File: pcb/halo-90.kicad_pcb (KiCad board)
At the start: 4 copper layers, 24 x 28.2 mm, 102 parts, among them J1 TC2030-SWIM-NL, U1 UFQFPN28, U3 DRV5032

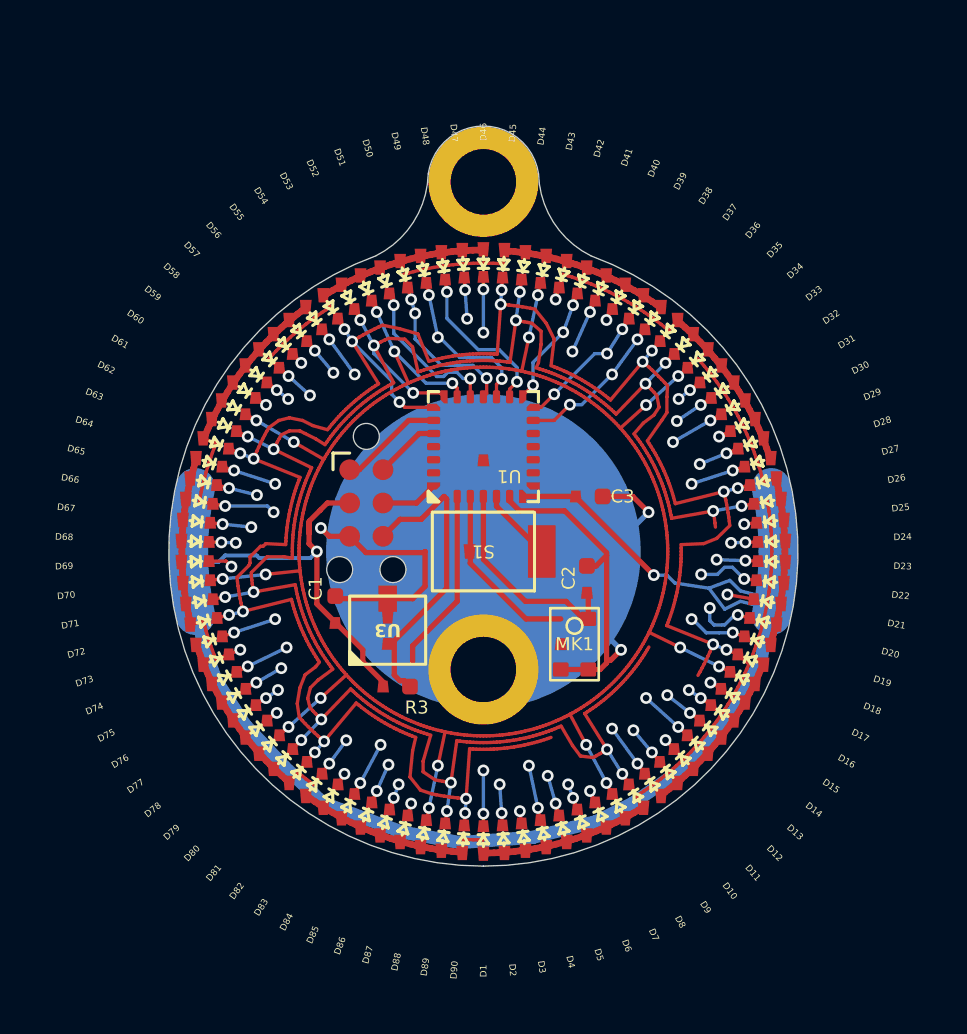
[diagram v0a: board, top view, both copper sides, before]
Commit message: feat(pcb): upgrade to KiCad 9, fix arc syntax, and standardize symbol libraries
- Updated halo.js gr_arc syntax to KiCad 9 (start/mid/end) point-based format.
- Standardized all 13 symbol libraries to KiCad 9 (version 20241209).
- Regenerated halo-90.kicad_pcb with correct formatting and net names.
- Verified file load compatibility.
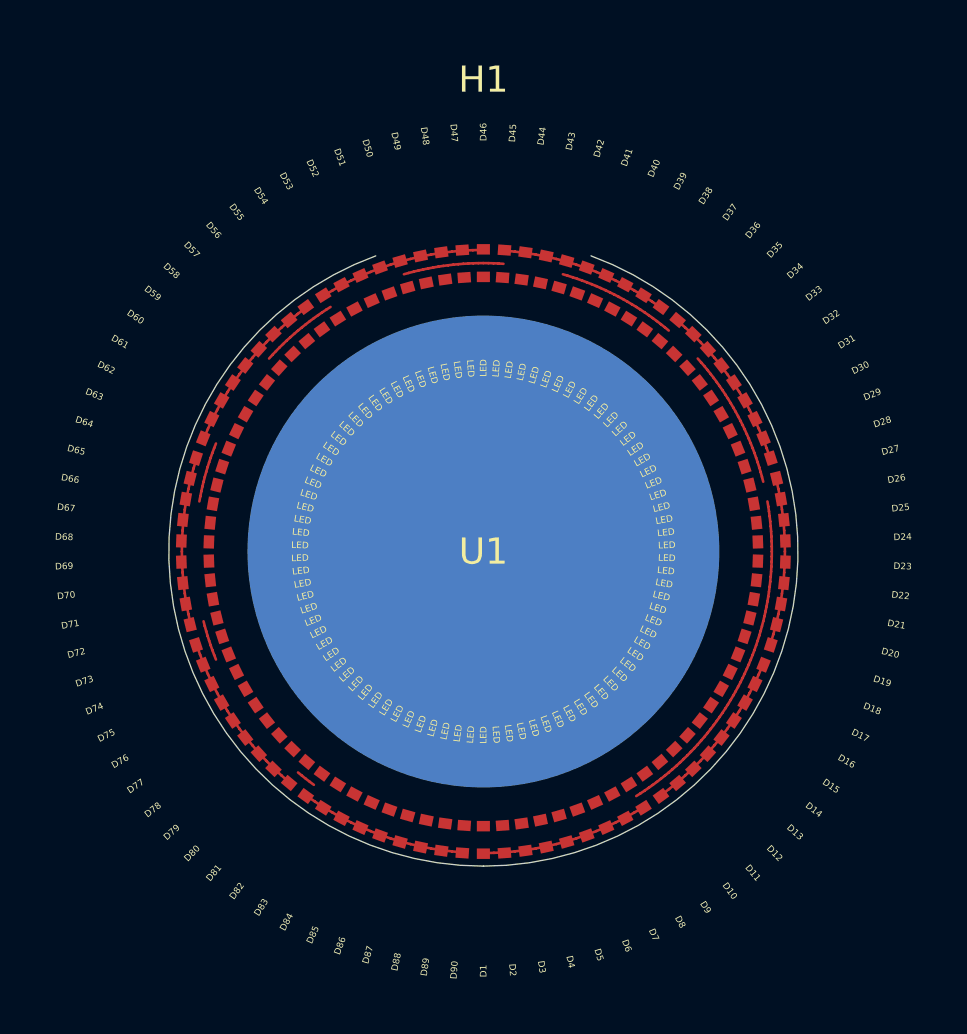
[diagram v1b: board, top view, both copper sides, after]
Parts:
- removed C1: 1u, passives:C-0402
- removed C2, C3: 100n, passives:C-0402
- removed H2: SMTSO1610MTJ, SMTSO1610MTJ:SMTSO1610MTJ
- removed J1: TC2030-SWIM-NL, TC2030-IDC-NL:Tag-Connect_TC2030-IDC-NL_2x03_P1.27mm_Vertical
- removed MK1: ZTS6216, ZTS6216:ZTS6216
- removed R3: 10k, passives:R-0402
- removed S1: TS-1088-AR02016, TS-1088-AR02016L:TS-1088-AR02016
- removed U3: DRV5032, DRV5032:DRV5032
- BT1: value CR-2032 -> CR2032
- H1: value SMTSO1610MTJ -> (none); footprint SMTSO1610MTJ:SMTSO1610MTJ -> earringHookWire:earringHookWire
- U1: value UFQFPN28 -> STM8L15xxx
- moved U1 4.00 mm to (0.00, 0.00), turned to 0 degrees
- moved H1 1.10 mm to (0.00, -13.0)
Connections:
- D1 pad 1: CPX-9 -> CPX-0
- D1 pad 2: CPX-0 -> CPX-9
- D10 pad 1: CPX-9 -> CPX-1
- D10 pad 2: CPX-1 -> CPX-9
- D11 pad 1: CPX-8 -> CPX-1
- D11 pad 2: CPX-1 -> CPX-8
- D12 pad 1: CPX-7 -> CPX-1
- D12 pad 2: CPX-1 -> CPX-7
- D13 pad 1: CPX-6 -> CPX-1
- D13 pad 2: CPX-1 -> CPX-6
- D14 pad 1: CPX-5 -> CPX-1
- D14 pad 2: CPX-1 -> CPX-5
- D15 pad 1: CPX-4 -> CPX-1
- D15 pad 2: CPX-1 -> CPX-4
- D16 pad 1: CPX-3 -> CPX-1
- D16 pad 2: CPX-1 -> CPX-3
- D17 pad 1: CPX-2 -> CPX-1
- D17 pad 2: CPX-1 -> CPX-2
- D18 pad 1: CPX-0 -> CPX-1
- D18 pad 2: CPX-1 -> CPX-0
- D19 pad 1: CPX-9 -> CPX-2
- D19 pad 2: CPX-2 -> CPX-9
- D2 pad 1: CPX-8 -> CPX-0
- D2 pad 2: CPX-0 -> CPX-8
- D20 pad 1: CPX-8 -> CPX-2
- D20 pad 2: CPX-2 -> CPX-8
- D21 pad 1: CPX-7 -> CPX-2
- D21 pad 2: CPX-2 -> CPX-7
- D22 pad 1: CPX-6 -> CPX-2
- D22 pad 2: CPX-2 -> CPX-6
- D23 pad 1: CPX-5 -> CPX-2
- D23 pad 2: CPX-2 -> CPX-5
- D24 pad 1: CPX-4 -> CPX-2
- D24 pad 2: CPX-2 -> CPX-4
- D25 pad 1: CPX-3 -> CPX-2
- D25 pad 2: CPX-2 -> CPX-3
- D26 pad 1: CPX-1 -> CPX-2
- D26 pad 2: CPX-2 -> CPX-1
- D27 pad 1: CPX-0 -> CPX-2
- D27 pad 2: CPX-2 -> CPX-0
- D28 pad 1: CPX-9 -> CPX-3
- D28 pad 2: CPX-3 -> CPX-9
- D29 pad 1: CPX-8 -> CPX-3
- D29 pad 2: CPX-3 -> CPX-8
- D3 pad 1: CPX-7 -> CPX-0
- D3 pad 2: CPX-0 -> CPX-7
- D30 pad 1: CPX-7 -> CPX-3
- D30 pad 2: CPX-3 -> CPX-7
- D31 pad 1: CPX-6 -> CPX-3
- D31 pad 2: CPX-3 -> CPX-6
- D32 pad 1: CPX-5 -> CPX-3
- D32 pad 2: CPX-3 -> CPX-5
- D33 pad 1: CPX-4 -> CPX-3
- D33 pad 2: CPX-3 -> CPX-4
- D34 pad 1: CPX-2 -> CPX-3
- D34 pad 2: CPX-3 -> CPX-2
- D35 pad 1: CPX-1 -> CPX-3
- D35 pad 2: CPX-3 -> CPX-1
- D36 pad 1: CPX-0 -> CPX-3
- D36 pad 2: CPX-3 -> CPX-0
- D37 pad 1: CPX-9 -> CPX-4
- D37 pad 2: CPX-4 -> CPX-9
- D38 pad 1: CPX-8 -> CPX-4
- D38 pad 2: CPX-4 -> CPX-8
- D39 pad 1: CPX-7 -> CPX-4
- D39 pad 2: CPX-4 -> CPX-7
- D4 pad 1: CPX-6 -> CPX-0
- D4 pad 2: CPX-0 -> CPX-6
- D40 pad 1: CPX-6 -> CPX-4
- D40 pad 2: CPX-4 -> CPX-6
- D41 pad 1: CPX-5 -> CPX-4
- D41 pad 2: CPX-4 -> CPX-5
- D42 pad 1: CPX-3 -> CPX-4
- D42 pad 2: CPX-4 -> CPX-3
- D43 pad 1: CPX-2 -> CPX-4
- D43 pad 2: CPX-4 -> CPX-2
- D44 pad 1: CPX-1 -> CPX-4
- D44 pad 2: CPX-4 -> CPX-1
- D45 pad 1: CPX-0 -> CPX-4
- D45 pad 2: CPX-4 -> CPX-0
- D46 pad 1: CPX-9 -> CPX-5
- D46 pad 2: CPX-5 -> CPX-9
- D47 pad 1: CPX-8 -> CPX-5
- D47 pad 2: CPX-5 -> CPX-8
- D48 pad 1: CPX-7 -> CPX-5
- D48 pad 2: CPX-5 -> CPX-7
- D49 pad 1: CPX-6 -> CPX-5
- D49 pad 2: CPX-5 -> CPX-6
- D5 pad 1: CPX-5 -> CPX-0
- D5 pad 2: CPX-0 -> CPX-5
- D50 pad 1: CPX-4 -> CPX-5
- D50 pad 2: CPX-5 -> CPX-4
- D51 pad 1: CPX-3 -> CPX-5
- D51 pad 2: CPX-5 -> CPX-3
- D52 pad 1: CPX-2 -> CPX-5
- D52 pad 2: CPX-5 -> CPX-2
- D53 pad 1: CPX-1 -> CPX-5
- D53 pad 2: CPX-5 -> CPX-1
- D54 pad 1: CPX-0 -> CPX-5
- D54 pad 2: CPX-5 -> CPX-0
- D55 pad 1: CPX-9 -> CPX-6
- D55 pad 2: CPX-6 -> CPX-9
- D56 pad 1: CPX-8 -> CPX-6
- D56 pad 2: CPX-6 -> CPX-8
- D57 pad 1: CPX-7 -> CPX-6
- D57 pad 2: CPX-6 -> CPX-7
- D58 pad 1: CPX-5 -> CPX-6
- D58 pad 2: CPX-6 -> CPX-5
- D59 pad 1: CPX-4 -> CPX-6
- D59 pad 2: CPX-6 -> CPX-4
- D6 pad 1: CPX-4 -> CPX-0
- D6 pad 2: CPX-0 -> CPX-4
- D60 pad 1: CPX-3 -> CPX-6
- D60 pad 2: CPX-6 -> CPX-3
- D61 pad 1: CPX-2 -> CPX-6
- D61 pad 2: CPX-6 -> CPX-2
- D62 pad 1: CPX-1 -> CPX-6
- D62 pad 2: CPX-6 -> CPX-1
- D63 pad 1: CPX-0 -> CPX-6
- D63 pad 2: CPX-6 -> CPX-0
- D64 pad 1: CPX-9 -> CPX-7
- D64 pad 2: CPX-7 -> CPX-9
- D65 pad 1: CPX-8 -> CPX-7
- D65 pad 2: CPX-7 -> CPX-8
- D66 pad 1: CPX-6 -> CPX-7
- D66 pad 2: CPX-7 -> CPX-6
- D67 pad 1: CPX-5 -> CPX-7
- D67 pad 2: CPX-7 -> CPX-5
- D68 pad 1: CPX-4 -> CPX-7
- D68 pad 2: CPX-7 -> CPX-4
- D69 pad 1: CPX-3 -> CPX-7
- D69 pad 2: CPX-7 -> CPX-3
- D7 pad 1: CPX-3 -> CPX-0
- D7 pad 2: CPX-0 -> CPX-3
- D70 pad 1: CPX-2 -> CPX-7
- D70 pad 2: CPX-7 -> CPX-2
- D71 pad 1: CPX-1 -> CPX-7
- D71 pad 2: CPX-7 -> CPX-1
- D72 pad 1: CPX-0 -> CPX-7
- D72 pad 2: CPX-7 -> CPX-0
- D73 pad 1: CPX-9 -> CPX-8
- D73 pad 2: CPX-8 -> CPX-9
- D74 pad 1: CPX-7 -> CPX-8
- D74 pad 2: CPX-8 -> CPX-7
- D75 pad 1: CPX-6 -> CPX-8
- D75 pad 2: CPX-8 -> CPX-6
- D76 pad 1: CPX-5 -> CPX-8
- D76 pad 2: CPX-8 -> CPX-5
- D77 pad 1: CPX-4 -> CPX-8
- D77 pad 2: CPX-8 -> CPX-4
- D78 pad 1: CPX-3 -> CPX-8
- D78 pad 2: CPX-8 -> CPX-3
- D79 pad 1: CPX-2 -> CPX-8
- D79 pad 2: CPX-8 -> CPX-2
- D8 pad 1: CPX-2 -> CPX-0
- D8 pad 2: CPX-0 -> CPX-2
- D80 pad 1: CPX-1 -> CPX-8
- D80 pad 2: CPX-8 -> CPX-1
- D81 pad 1: CPX-0 -> CPX-8
- D81 pad 2: CPX-8 -> CPX-0
- D82 pad 1: CPX-8 -> CPX-9
- D82 pad 2: CPX-9 -> CPX-8
- D83 pad 1: CPX-7 -> CPX-9
- D83 pad 2: CPX-9 -> CPX-7
- D84 pad 1: CPX-6 -> CPX-9
- D84 pad 2: CPX-9 -> CPX-6
- D85 pad 1: CPX-5 -> CPX-9
- D85 pad 2: CPX-9 -> CPX-5
- D86 pad 1: CPX-4 -> CPX-9
- D86 pad 2: CPX-9 -> CPX-4
- D87 pad 1: CPX-3 -> CPX-9
- D87 pad 2: CPX-9 -> CPX-3
- D88 pad 1: CPX-2 -> CPX-9
- D88 pad 2: CPX-9 -> CPX-2
- D89 pad 1: CPX-1 -> CPX-9
- D89 pad 2: CPX-9 -> CPX-1
- D9 pad 1: CPX-1 -> CPX-0
- D9 pad 2: CPX-0 -> CPX-1
- D90 pad 1: CPX-0 -> CPX-9
- D90 pad 2: CPX-9 -> CPX-0
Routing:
- net CPX-8: track 106.9 -> 7.96 mm, vias 19 -> 0
- net CPX-0: track 101.2 -> 6.42 mm, vias 19 -> 0
- net CPX-7: track 99.3 -> 8.73 mm, vias 10 -> 0
- net CPX-3: track 101.1 -> 11.8 mm, vias 10 -> 0
- net CPX-4: track 98.1 -> 11.0 mm, vias 19 -> 0
- net CPX-1: track 99.4 -> 13.3 mm, vias 19 -> 0
- net CPX-5: track 95.7 -> 10.3 mm, vias 19 -> 0
- net CPX-9: track 87.5 -> 7.19 mm, vias 19 -> 0
- net CPX-6: track 89.7 -> 9.49 mm, vias 19 -> 0
- net CPX-2: track 91.5 -> 12.6 mm, vias 19 -> 0
- net +3V: track 67.6 -> 0.00 mm, vias 2 -> 0
- net GND: track 44.0 -> 0.00 mm, vias 3 -> 0
- net RST: track 11.4 -> 0.00 mm
- net MIC_PWR: track 8.38 -> 0.00 mm
- net HALL: track 7.00 -> 0.00 mm
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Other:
- board size 24 x 28.2 mm -> 24 x 23.3 mm
- net class Default added: clearance 0.1, trace_width 0.1, via_dia 0.45, via_drill 0.25
- rule pad_to_mask_clearance: 0 -> 0.05
- board text removed: "KOLIBRI sawaiz 2026-02 HALO-90 0v7"

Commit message: pcb: upgrade to KiCad 9 format with elegant curved fan-out routing
- Synchronized netlist with schematic source of truth
- Implemented mathematically elegant circular arc trace paths in halo.js
- Standardized symbol libraries and PCB format to KiCad 9 (20241229)
- Corrected gr_arc syntax and added mandatory timestamps for segments/vias
- Updated README.md with design intentions and programmatic layout details
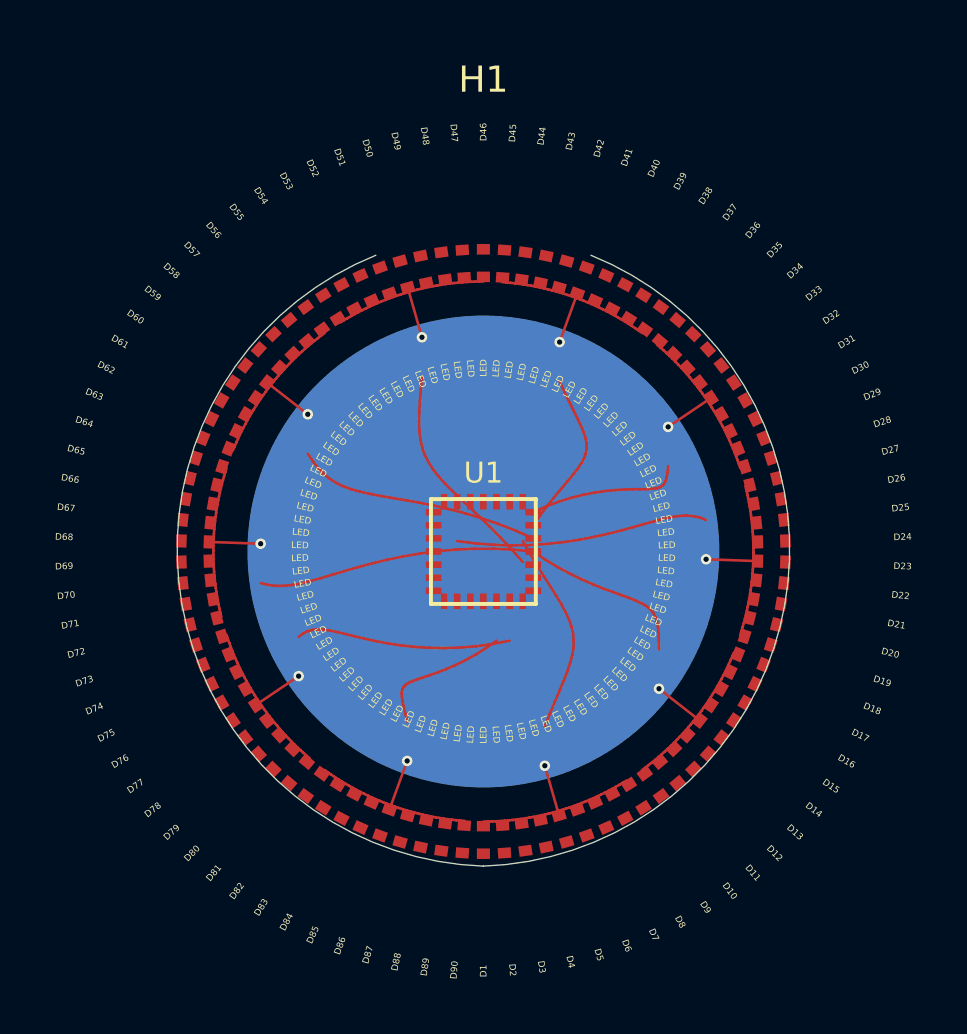
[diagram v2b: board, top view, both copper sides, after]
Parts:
- U1: value STM8L15xxx -> STM8L151G6
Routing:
- net CPX-7: track 8.73 -> 18.1 mm, vias 0 -> 1
- net CPX-0: track 6.42 -> 15.3 mm, vias 0 -> 1
- net CPX-8: track 7.96 -> 15.8 mm, vias 0 -> 1
- net CPX-6: track 9.49 -> 17.0 mm, vias 0 -> 1
- net CPX-5: track 10.3 -> 16.1 mm, vias 0 -> 1
- net CPX-9: track 7.19 -> 12.9 mm, vias 0 -> 1
- net CPX-2: track 12.6 -> 17.2 mm, vias 0 -> 1
- net CPX-4: track 11.0 -> 13.9 mm, vias 0 -> 1
- net CPX-3: track 11.8 -> 13.4 mm, vias 0 -> 1
- net CPX-1: track 13.3 -> 14.2 mm, vias 0 -> 1
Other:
- board size 24 x 23.3 mm -> 23.4 x 23.3 mm
- net class Default: via_dia 0.45 -> 0.4; via_drill 0.25 -> 0.2

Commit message: pcb: aesthetic redesign with circular fan-out as jewelry artwork
- Restored original component placements (Button S1, Mic MK1, MCU U1 at 0,-4)
- Implemented high-resolution circular spiral routing for MCU fan-out
- Reduced trace width to 0.1mm and de-cluttered reference text
- Added 3D model STP references for LEDs and MCU
- Verified netlist and KiCad 9 compatibility
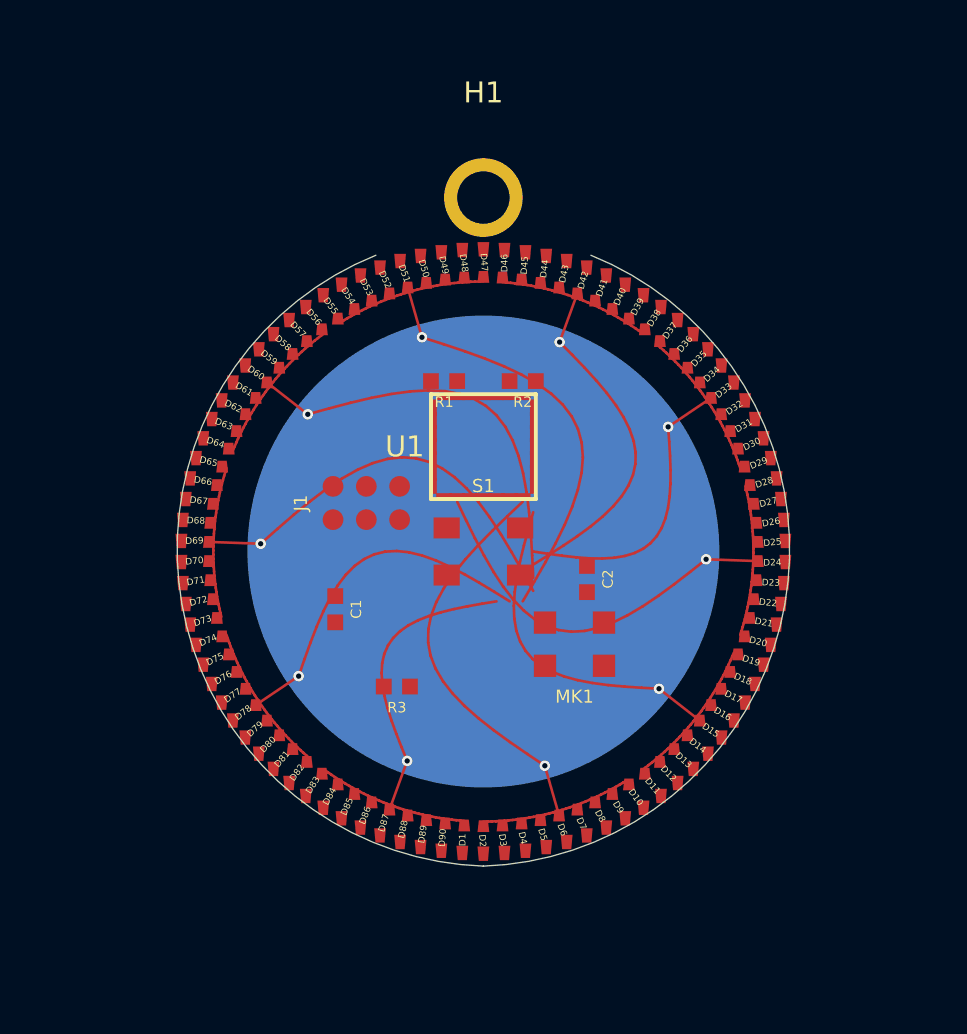
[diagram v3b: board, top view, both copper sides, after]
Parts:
- added C1: , passives:C-0402, F.Cu at (-5.65, 2.20)
- added C2: , passives:C-0402, F.Cu at (3.95, 1.05)
- added J1: , TC2030-IDC-NL:Tag-Connect_TC2030-IDC-NL_2x03_P1.27mm_Vertical, F.Cu at (-4.46, -1.85)
- added MK1: , ZTS6216:ZTS6216, F.Cu at (3.48, 3.54)
- added R1: , passives:R-0402, F.Cu at (-1.50, -6.50)
- added R2: , passives:R-0402, F.Cu at (1.50, -6.50)
- added R3: , passives:R-0402, F.Cu at (-3.30, 5.15)
- added S1: , TS-1088-AR02016L:TS-1088-AR02016, F.Cu at (0.00, 0.00)
- BT1: value CR2032 -> (none)
- D1, D10, D11, D12, D13, D14, D15, D16, D17, D18, D19, D2, D20, D21, D22, D23, D24, D25, D26, D27, D28, D29, D3, D30, D31, D32, D33, D34, D35, D36, D37, D38, D39, D4, D40, D41, D42, D43, D44, D45, D46, D47, D48, D49, D5, D50, D51, D52, D53, D54, D55, D56, D57, D58, D59, D6, D60, D61, D62, D63, D64, D65, D66, D67, D68, D69, D7, D70, D71, D72, D73, D74, D75, D76, D77, D78, D79, D8, D80, D81, D82, D83, D84, D85, D86, D87, D88, D89, D9, D90: value LED -> (none)
- H1: footprint earringHookWire:earringHookWire -> tooling:TestPoint_Pad_D4.0mm
- moved U1 4.00 mm to (0.00, -4.00), turned to 90 degrees
- moved H1 0.50 mm to (0.00, -13.5)
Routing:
- net CPX-5: track 16.1 -> 21.8 mm
- net CPX-0: track 15.3 -> 20.9 mm
- net CPX-4: track 13.9 -> 18.8 mm
- net CPX-6: track 17.0 -> 21.6 mm
- net CPX-1: track 14.2 -> 18.5 mm
- net CPX-9: track 12.9 -> 16.8 mm
- net CPX-3: track 13.4 -> 16.8 mm
- net CPX-7: track 18.1 -> 21.5 mm
- net CPX-2: track 17.2 -> 20.4 mm
- net CPX-8: track 15.8 -> 18.8 mm
